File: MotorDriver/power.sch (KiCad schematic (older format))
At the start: 16 parts, among them J10 PWR_D, J8 Vbat, J9 GND, U1 L78L05_SOT89, U2 L78L33_SOT89

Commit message: Finished printable parts
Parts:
- D1: footprint Diode_SMD:D_SMA -> Diode_SMD:D_SMA-SMB_Universal_Handsoldering
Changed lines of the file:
@@
 F 0 "D1" H 2700 2084 50  0000 C CNN
 F 1 "MRA4003T3G" H 2700 2175 50  0000 C CNN
-F 2 "Diode_SMD:D_SMA" H 2700 2125 50  0001 C CNN
+F 2 "Diode_SMD:D_SMA-SMB_Universal_Handsoldering" H 2700 2125 50  0001 C CNN
 F 3 "http://www.onsemi.com/pub_link/Collateral/MRA4003T3-D.PDF" H 2700 2300 50  0001 C CNN
 	1    2700 2300

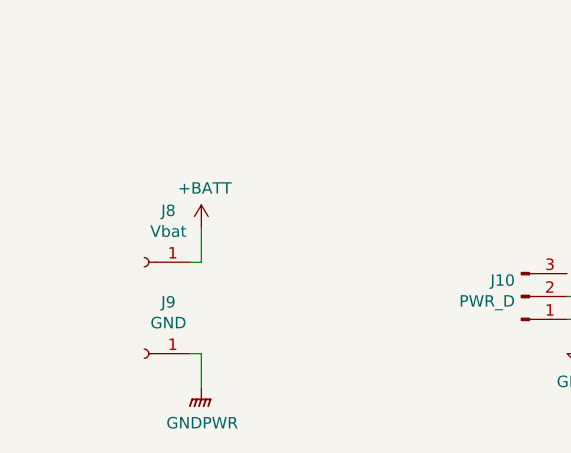
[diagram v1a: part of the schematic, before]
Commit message: Power and output ping changed roblaced by holes. Correction of tracks width and vias diameters.
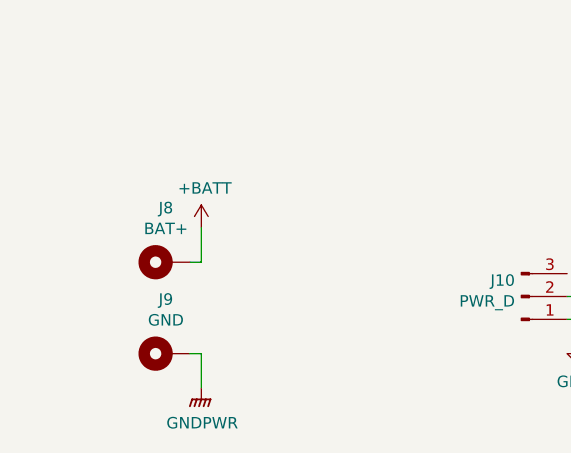
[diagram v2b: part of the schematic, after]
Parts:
- removed J8: Vbat, Connector_Pin:Pin_D1.4mm_L8.5mm_W2.8mm_FlatFork, symbol Connector:Conn_01x01_Female
- removed J9: GND, Connector_Pin:Pin_D1.4mm_L8.5mm_W2.8mm_FlatFork, symbol Connector:Conn_01x01_Female
- added J8: BAT+, MountingHole:MountingHole_2.2mm_M2_Pad_Via, symbol Mechanical:MountingHole_Pad
- added J9: GND, MountingHole:MountingHole_2.2mm_M2_Pad_Via, symbol Mechanical:MountingHole_Pad
- JP1: footprint Jumper:SolderJumper-2_P1.3mm_Bridged_RoundedPad1.0x1.5mm -> Jumper:SolderJumper-2_P1.3mm_Open_RoundedPad1.0x1.5mm
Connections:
- net +BATT: now also J8.1
- net GNDPWR: now also J9.1
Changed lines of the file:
@@
 F 0 "JP1" H 5050 4612 50  0000 C CNN
 F 1 "Jumper_NC_Small" H 5050 4521 50  0000 C CNN
-F 2 "Jumper:SolderJumper-2_P1.3mm_Bridged_RoundedPad1.0x1.5mm" H 5050 4400 50  0001 C CNN
+F 2 "Jumper:SolderJumper-2_P1.3mm_Open_RoundedPad1.0x1.5mm" H 5050 4400 50  0001 C CNN
 F 3 "~" H 5050 4400 50  0001 C CNN
 	1    5050 4400
@@
 	3250 4400 3850 4400
 $Comp
-L Connector:Conn_01x01_Female J8
-U 1 1 5C466EF8
-P 2450 5750
-F 0 "J8" H 2344 5525 50  0000 C CNN
-F 1 "Vbat" H 2344 5616 50  0000 C CNN
-F 2 "Connector_Pin:Pin_D1.4mm_L8.5mm_W2.8mm_FlatFork" H 2450 5750 50  0001 C CNN
-F 3 "~" H 2450 5750 50  0001 C CNN
-	1    2450 5750
-	-1   0    0    1
-$EndComp
-$Comp
-L Connector:Conn_01x01_Female J9
-U 1 1 5C46711F
-P 2450 6150
-F 0 "J9" H 2344 5925 50  0000 C CNN
-F 1 "GND" H 2344 6016 50  0000 C CNN
-F 2 "Connector_Pin:Pin_D1.4mm_L8.5mm_W2.8mm_FlatFork" H 2450 6150 50  0001 C CNN
-F 3 "~" H 2450 6150 50  0001 C CNN
-	1    2450 6150
-	-1   0    0    1
-$EndComp
-$Comp
 L power:GNDPWR #PWR0147
 U 1 1 5C467237
@@
 Text Label 3150 2300 0    50   ~ 0
 pwrs_in
+$Comp
+L Mechanical:MountingHole_Pad J8
+U 1 1 5C4C9A30
+P 2550 5750
+F 0 "J8" V 2787 5755 50  0000 C CNN
+F 1 "BAT+" V 2696 5755 50  0000 C CNN
+F 2 "MountingHole:MountingHole_2.2mm_M2_Pad_Via" H 2550 5750 50  0001 C CNN
+F 3 "~" H 2550 5750 50  0001 C CNN
+	1    2550 5750
+	0    -1   -1   0
+$EndComp
+$Comp
+L Mechanical:MountingHole_Pad J9
+U 1 1 5C4C9ACE
+P 2550 6150
+F 0 "J9" V 2787 6155 50  0000 C CNN
+F 1 "GND" V 2696 6155 50  0000 C CNN
+F 2 "MountingHole:MountingHole_2.2mm_M2_Pad_Via" H 2550 6150 50  0001 C CNN
+F 3 "~" H 2550 6150 50  0001 C CNN
+	1    2550 6150
+	0    -1   -1   0
+$EndComp
 $EndSCHEMATC

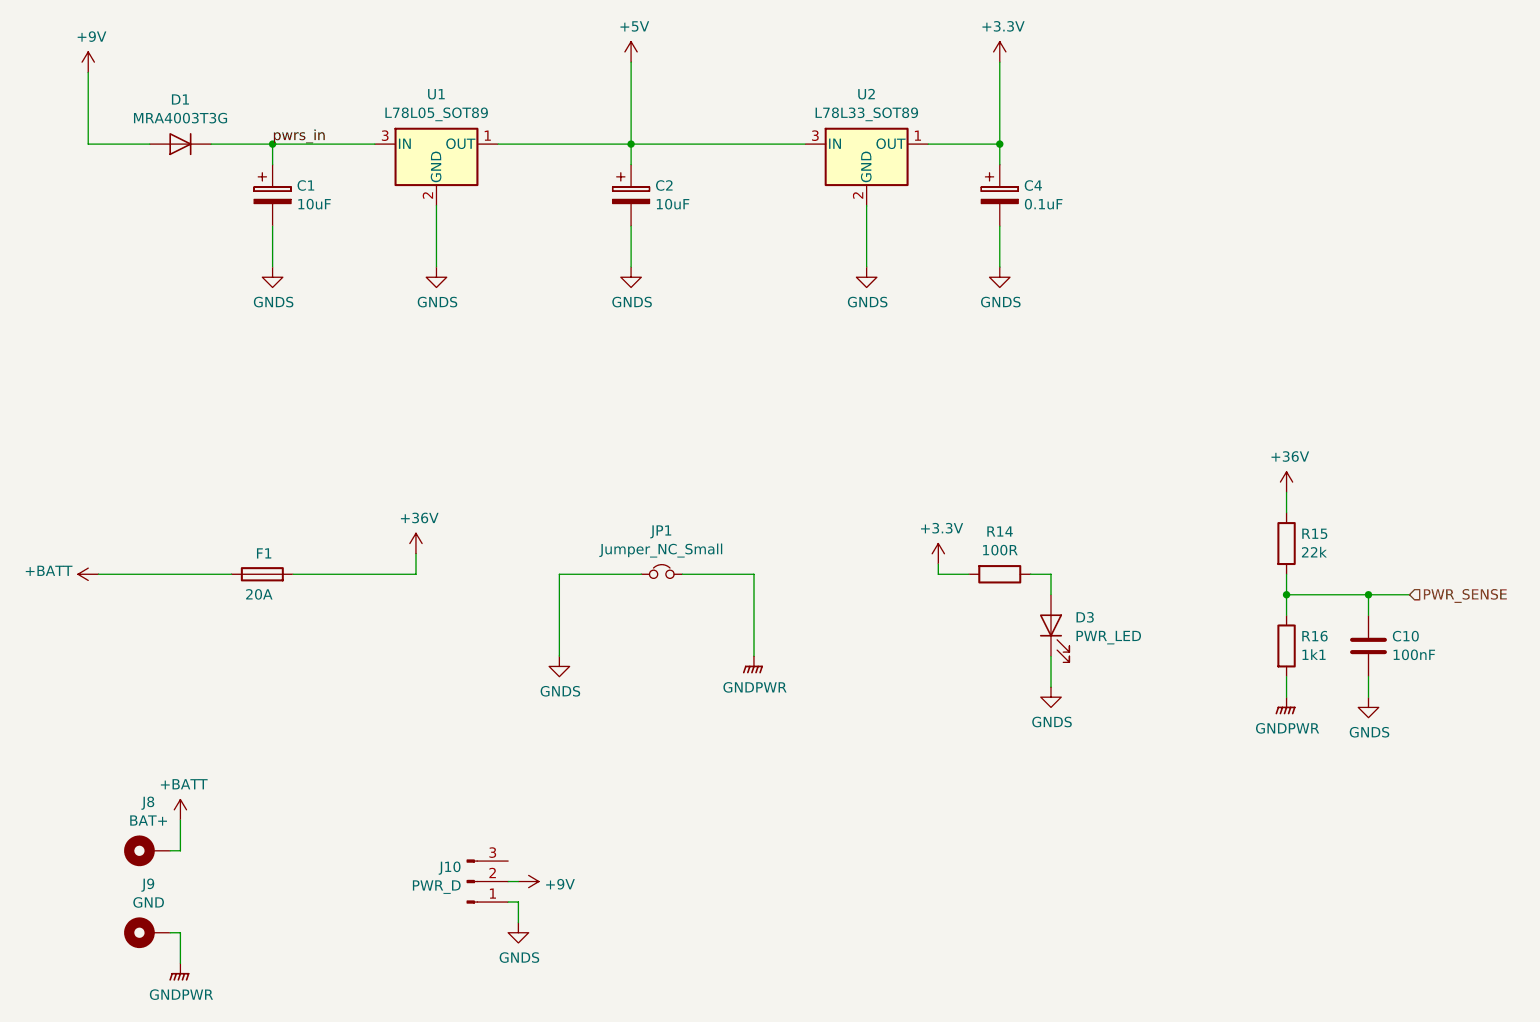
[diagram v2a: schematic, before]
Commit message: Added filter capacitors to low votlage power supply
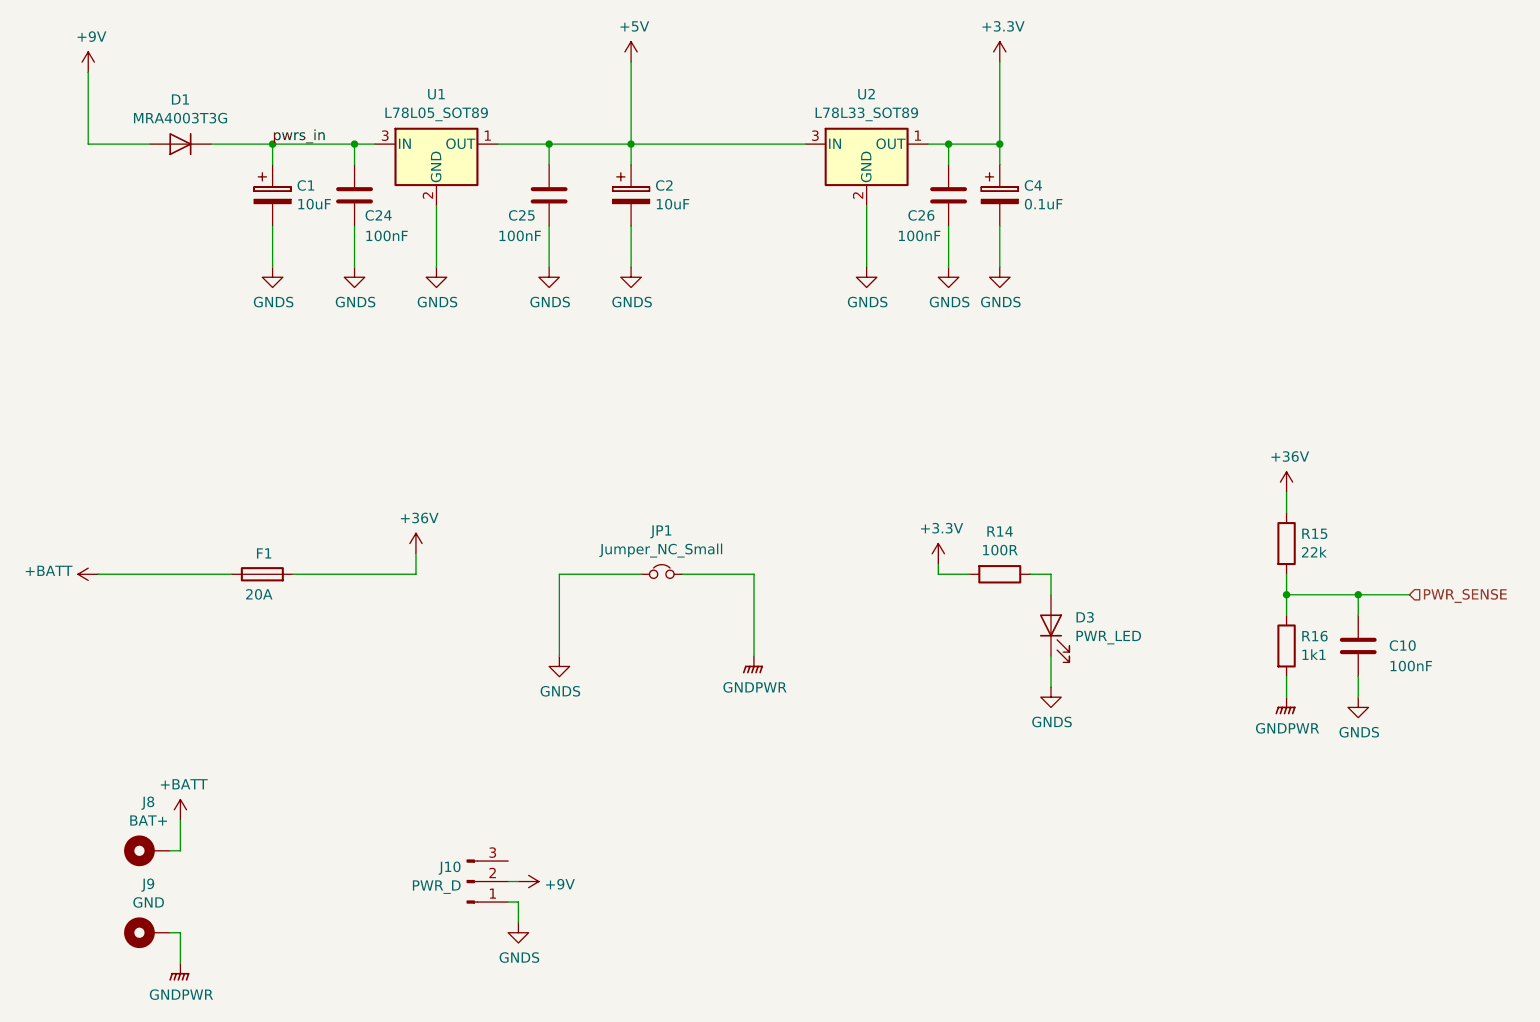
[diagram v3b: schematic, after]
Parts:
- added C24, C25, C26: 100nF, Capacitor_SMD:C_0603_1608Metric_Pad1.05x0.95mm_HandSolder, symbol Device:C
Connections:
- net +3V3: now also C26.1
- net +5V: now also C25.1
- net GNDS: now also C24.2, C25.2, C26.2
- net pwrs_in: now also C24.1
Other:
- moved on the sheet: C10
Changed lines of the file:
@@
 	4900 2300 5750 2300
 Wire Wire Line
-	6350 2300 6700 2300
+	6350 2300 6450 2300
 Wire Wire Line
 	6700 2300 6700 2400
@@
 	3150 2700 3150 2900
 Wire Wire Line
-	4250 2300 4900 2300
-Wire Wire Line
 	3950 2600 3950 2900
 Wire Wire Line
@@
 	3150 2400 3150 2300
 Connection ~ 3150 2300
-Wire Wire Line
-	3150 2300 3650 2300
 Wire Wire Line
 	2250 1950 2250 2300
@@
 L Device:C C10
 U 1 1 5C487B0F
-P 8500 4750
-F 0 "C10" H 8615 4796 50  0000 L CNN
-F 1 "100nF" H 8615 4705 50  0000 L CNN
-F 2 "Capacitor_SMD:C_0603_1608Metric_Pad1.05x0.95mm_HandSolder" H 8538 4600 50  0001 C CNN
-F 3 "~" H 8500 4750 50  0001 C CNN
-	1    8500 4750
-	1    0    0    -1
-$EndComp
-Wire Wire Line
-	8100 4500 8500 4500
-Wire Wire Line
-	8500 4600 8500 4500
-Connection ~ 8500 4500
-Wire Wire Line
-	8500 4500 8700 4500
+P 8450 4750
+F 0 "C10" H 8600 4750 50  0000 L CNN
+F 1 "100nF" H 8600 4650 50  0000 L CNN
+F 2 "Capacitor_SMD:C_0603_1608Metric_Pad1.05x0.95mm_HandSolder" H 8488 4600 50  0001 C CNN
+F 3 "~" H 8450 4750 50  0001 C CNN
+	1    8450 4750
+	1    0    0    -1
+$EndComp
+Wire Wire Line
+	6450 2400 6450 2300
 $Comp
 L power:GNDS #PWR0154
 U 1 1 5C4889D1
-P 8500 5000
-F 0 "#PWR0154" H 8500 4750 50  0001 C CNN
-F 1 "GNDS" H 8505 4827 50  0000 C CNN
-F 2 "" H 8500 5000 50  0001 C CNN
-F 3 "" H 8500 5000 50  0001 C CNN
-	1    8500 5000
-	1    0    0    -1
-$EndComp
-Wire Wire Line
-	8500 5000 8500 4900
+P 8450 5000
+F 0 "#PWR0154" H 8450 4750 50  0001 C CNN
+F 1 "GNDS" H 8455 4827 50  0000 C CNN
+F 2 "" H 8450 5000 50  0001 C CNN
+F 3 "" H 8450 5000 50  0001 C CNN
+	1    8450 5000
+	1    0    0    -1
+$EndComp
 Text Label 3150 2300 0    50   ~ 0
 pwrs_in
@@
 	0    -1   -1   0
 $EndComp
+Wire Wire Line
+	3150 2300 3550 2300
+Connection ~ 6450 2300
+Wire Wire Line
+	6450 2300 6700 2300
+Wire Wire Line
+	4250 2300 4500 2300
+$Comp
+L Device:C C26
+U 1 1 5C4D0CB3
+P 6450 2550
+F 0 "C26" H 6250 2450 50  0000 L CNN
+F 1 "100nF" H 6200 2350 50  0000 L CNN
+F 2 "Capacitor_SMD:C_0603_1608Metric_Pad1.05x0.95mm_HandSolder" H 6488 2400 50  0001 C CNN
+F 3 "~" H 6450 2550 50  0001 C CNN
+	1    6450 2550
+	1    0    0    -1
+$EndComp
+$Comp
+L power:GNDS #PWR0161
+U 1 1 5C4D0CB9
+P 6450 2900
+F 0 "#PWR0161" H 6450 2650 50  0001 C CNN
+F 1 "GNDS" H 6455 2727 50  0000 C CNN
+F 2 "" H 6450 2900 50  0001 C CNN
+F 3 "" H 6450 2900 50  0001 C CNN
+	1    6450 2900
+	1    0    0    -1
+$EndComp
+Wire Wire Line
+	6450 2700 6450 2900
+Wire Wire Line
+	8450 4900 8450 5000
+Wire Wire Line
+	8100 4500 8450 4500
+Wire Wire Line
+	8450 4600 8450 4500
+Connection ~ 8450 4500
+Wire Wire Line
+	8450 4500 8700 4500
+$Comp
+L Device:C C25
+U 1 1 5C4D38DE
+P 4500 2550
+F 0 "C25" H 4300 2450 50  0000 L CNN
+F 1 "100nF" H 4250 2350 50  0000 L CNN
+F 2 "Capacitor_SMD:C_0603_1608Metric_Pad1.05x0.95mm_HandSolder" H 4538 2400 50  0001 C CNN
+F 3 "~" H 4500 2550 50  0001 C CNN
+	1    4500 2550
+	1    0    0    -1
+$EndComp
+$Comp
+L power:GNDS #PWR0162
+U 1 1 5C4D38E4
+P 4500 2900
+F 0 "#PWR0162" H 4500 2650 50  0001 C CNN
+F 1 "GNDS" H 4505 2727 50  0000 C CNN
+F 2 "" H 4500 2900 50  0001 C CNN
+F 3 "" H 4500 2900 50  0001 C CNN
+	1    4500 2900
+	1    0    0    -1
+$EndComp
+Wire Wire Line
+	4500 2700 4500 2900
+$Comp
+L Device:C C24
+U 1 1 5C4D4290
+P 3550 2550
+F 0 "C24" H 3600 2450 50  0000 L CNN
+F 1 "100nF" H 3600 2350 50  0000 L CNN
+F 2 "Capacitor_SMD:C_0603_1608Metric_Pad1.05x0.95mm_HandSolder" H 3588 2400 50  0001 C CNN
+F 3 "~" H 3550 2550 50  0001 C CNN
+	1    3550 2550
+	1    0    0    -1
+$EndComp
+$Comp
+L power:GNDS #PWR0163
+U 1 1 5C4D4296
+P 3550 2900
+F 0 "#PWR0163" H 3550 2650 50  0001 C CNN
+F 1 "GNDS" H 3555 2727 50  0000 C CNN
+F 2 "" H 3550 2900 50  0001 C CNN
+F 3 "" H 3550 2900 50  0001 C CNN
+	1    3550 2900
+	1    0    0    -1
+$EndComp
+Wire Wire Line
+	3550 2700 3550 2900
+Wire Wire Line
+	4500 2400 4500 2300
+Connection ~ 4500 2300
+Wire Wire Line
+	4500 2300 4900 2300
+Wire Wire Line
+	3550 2400 3550 2300
+Connection ~ 3550 2300
+Wire Wire Line
+	3550 2300 3650 2300
 $EndSCHEMATC
